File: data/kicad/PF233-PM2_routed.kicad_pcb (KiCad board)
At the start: 4 copper layers, 28 x 70 mm, 17 parts, among them J1 MT60-M leads: BAT+ BAT- ILK, J3 Power switch pair (top housin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, Q1 Si4401FDY -40V

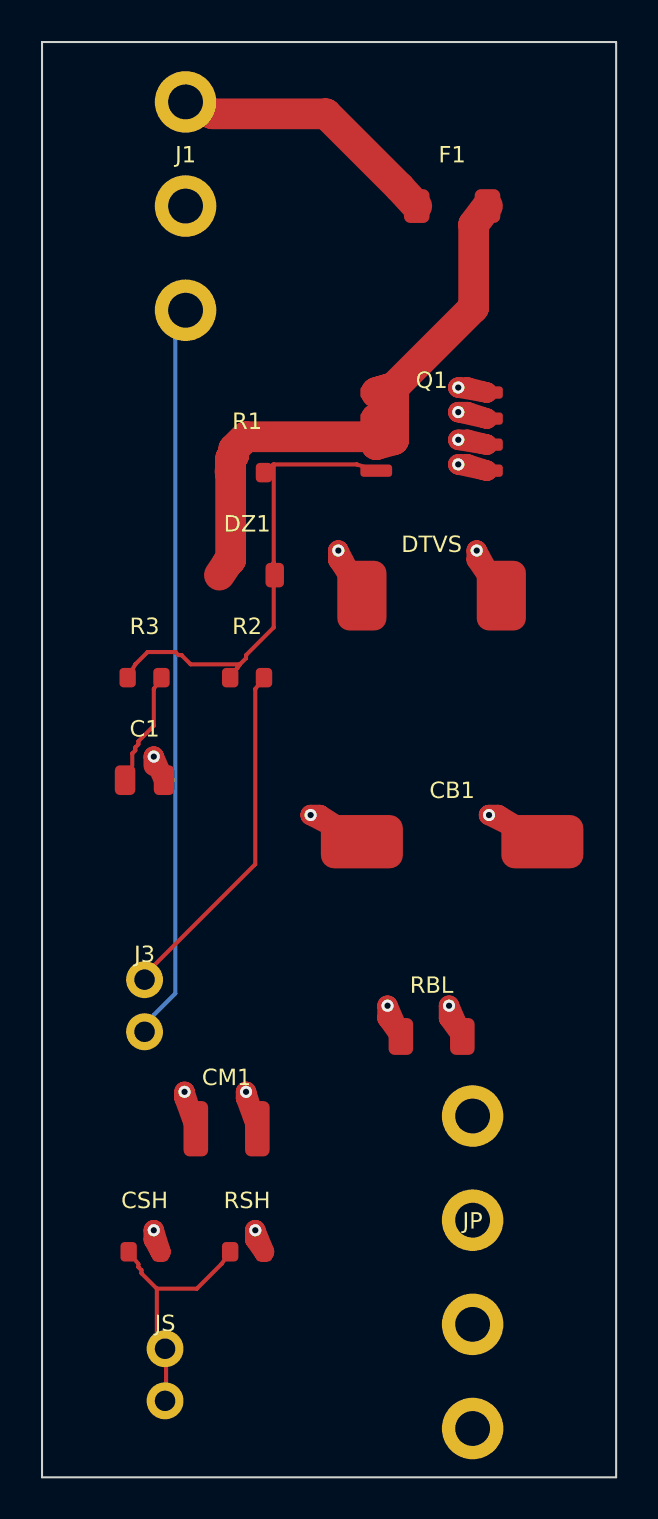
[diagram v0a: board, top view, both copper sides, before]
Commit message: WIP (NOT signed off): data published by the first close-out sign-off run, which had 5 FAIL (CB1D-C2 / AU1 fine-pitch clearance); superseded by the rerun in progress
Co-Authored-By: Claude Opus 5.5 <noreply@anthropic.com>
Claude-Session: https://claude.ai/code/session_01FX4DWSYYjMCFGGA6gmha65
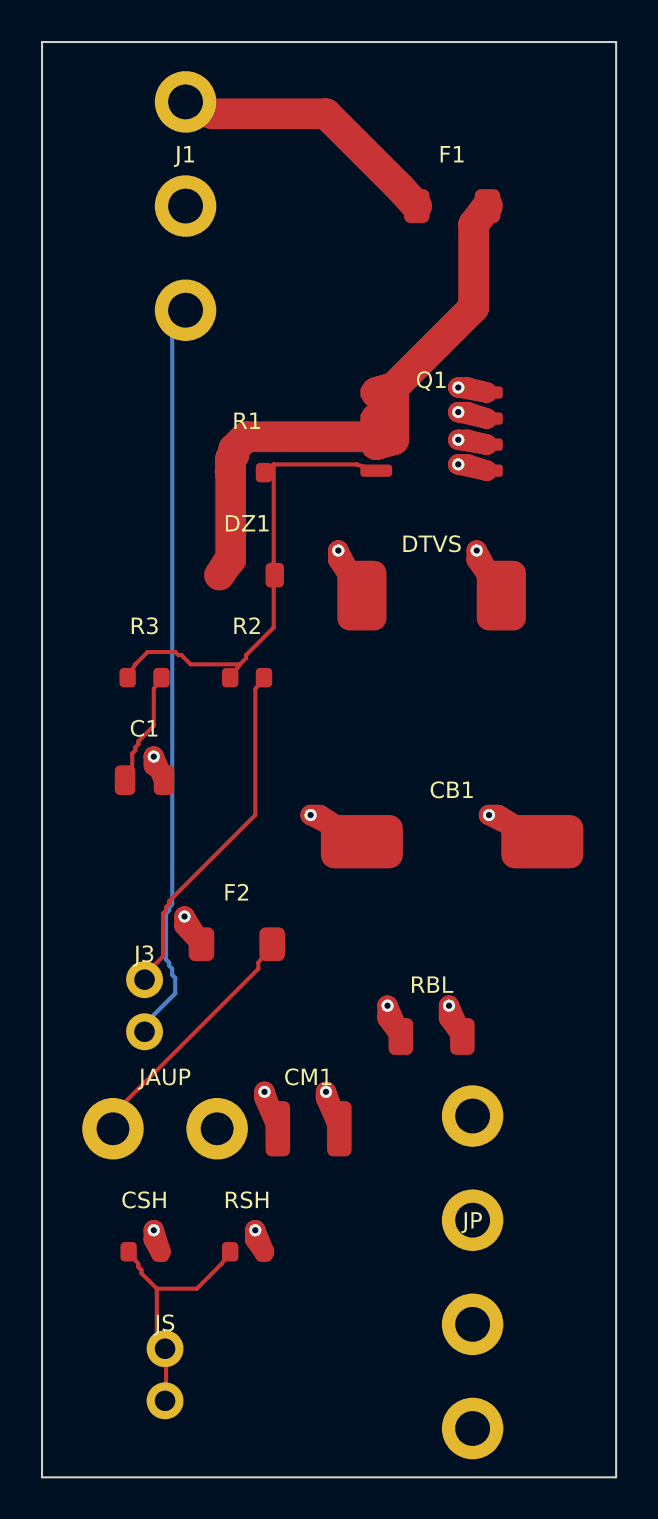
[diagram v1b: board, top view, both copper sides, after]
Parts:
- added F2: 0.5A slow 32V, Fuse:Fuse_1206_3216Metric, F.Cu at (95.5, 109.0)
- added JAUP: Power to AU1: VBUS_AU, GND, Connector:SolderPad_2x_P5.08mm, F.Cu at (92.0, 118.0)
- moved CM1 4.00 mm to (99.0, 118.0)
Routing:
- net VBUS_AU: track 0.00 -> 12.0 mm
- net VBUS: track 31.0 -> 34.3 mm, vias 9 -> 10
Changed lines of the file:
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@@
   (net 8 "SW_A")
   (net 9 "VBUS")
+  (net 10 "VBUS_AU")
   (footprint "Connector:Wire_pads_1x3_P5.08mm" (layer "F.Cu") (at 93.0000 73.0000)
     (property "Reference" "J1" (at 0 -2.5 0) (layer "F.SilkS") (effects (font (size 0.8 0.8) (thickness 0.12))))
@@
     (pad "2" smd roundrect (at 4.400 0.000) (size 4.000 2.600) (layers "F.Cu" "F.Paste" "F.Mask") (net 3 "GND"))
   )
-  (footprint "Capacitor_SMD:C_1210_3225Metric" (layer "F.Cu") (at 95.0000 118.0000)
+  (footprint "Capacitor_SMD:C_1210_3225Metric" (layer "F.Cu") (at 99.0000 118.0000)
     (property "Reference" "CM1" (at 0 -2.5 0) (layer "F.SilkS") (effects (font (size 0.8 0.8) (thickness 0.12))))
     (property "Value" "10u 50V" (at 0 2.5 0) (layer "F.Fab") (effects (font (size 0.8 0.8) (thickness 0.12))))
@@
     (pad "1" smd roundrect (at -1.500 0.000) (size 1.200 1.800) (layers "F.Cu" "F.Paste" "F.Mask") (net 9 "VBUS"))
     (pad "2" smd roundrect (at 1.500 0.000) (size 1.200 1.800) (layers "F.Cu" "F.Paste" "F.Mask") (net 3 "GND"))
+  )
+  (footprint "Fuse:Fuse_1206_3216Metric" (layer "F.Cu") (at 95.5000 109.0000)
+    (property "Reference" "F2" (at 0 -2.5 0) (layer "F.SilkS") (effects (font (size 0.8 0.8) (thickness 0.12))))
+    (property "Value" "0.5A slow 32V" (at 0 2.5 0) (layer "F.Fab") (effects (font (size 0.8 0.8) (thickness 0.12))))
+    (attr smd)
+    (model "${KIPRJMOD}/3dmodels/PF233_FUSE1206B.wrl" (offset (xyz 0 0 0)) (scale (xyz 0.3937 0.3937 0.3937)) (rotate (xyz 0 0 0)))
+    (pad "1" smd roundrect (at -1.725 0.000) (size 1.250 1.650) (layers "F.Cu" "F.Paste" "F.Mask") (net 9 "VBUS"))
+    (pad "2" smd roundrect (at 1.725 0.000) (size 1.250 1.650) (layers "F.Cu" "F.Paste" "F.Mask") (net 10 "VBUS_AU"))
+  )
+  (footprint "Connector:SolderPad_2x_P5.08mm" (layer "F.Cu") (at 92.0000 118.0000)
+    (property "Reference" "JAUP" (at 0 -2.5 0) (layer "F.SilkS") (effects (font (size 0.8 0.8) (thickness 0.12))))
+    (property "Value" "Power to AU1: VBUS_AU, GND" (at 0 2.5 0) (layer "F.Fab") (effects (font (size 0.8 0.8) (thickness 0.12))))
+    (attr through_hole)
+    (pad "1" thru_hole circle (at -2.540 0.000) (size 3.0 3.0) (drill 1.6) (layers "*.Cu" "*.Mask") (net 10 "VBUS_AU"))
+    (pad "2" thru_hole circle (at 2.540 0.000) (size 3.0 3.0) (drill 1.6) (layers "*.Cu" "*.Mask") (net 3 "GND"))
   )
   (footprint "Connector:Wire_pads_1x4_P5.08mm" (layer "F.Cu") (at 107.0000 125.0000)
@@
   (segment (start 108.2500 102.7000) (end 107.8000 102.7000) (width 1.0) (layer "F.Cu") (net 3))
   (segment (start 107.8000 102.7000) (end 110.4000 104.0000) (width 1.0) (layer "F.Cu") (net 3))
-  (segment (start 96.5000 118.0000) (end 95.9500 116.5000) (width 1.0) (layer "F.Cu") (net 3))
-  (segment (start 95.9500 116.5000) (end 95.9500 116.2000) (width 1.0) (layer "F.Cu") (net 3))
-  (segment (start 95.9500 116.2000) (end 96.5000 118.0000) (width 1.0) (layer "F.Cu") (net 3))
+  (segment (start 100.5000 118.0000) (end 99.8500 116.5000) (width 1.0) (layer "F.Cu") (net 3))
+  (segment (start 99.8500 116.5000) (end 99.8500 116.2000) (width 1.0) (layer "F.Cu") (net 3))
+  (segment (start 99.8500 116.2000) (end 100.5000 118.0000) (width 1.0) (layer "F.Cu") (net 3))
   (segment (start 106.5000 113.5000) (end 105.8500 112.6000) (width 1.0) (layer "F.Cu") (net 3))
   (segment (start 105.8500 112.6000) (end 105.8500 112.0000) (width 1.0) (layer "F.Cu") (net 3))
@@
   (segment (start 99.5500 102.7000) (end 99.1000 102.7000) (width 1.0) (layer "F.Cu") (net 9))
   (segment (start 99.1000 102.7000) (end 101.6000 104.0000) (width 1.0) (layer "F.Cu") (net 9))
-  (segment (start 93.5000 118.0000) (end 92.9500 116.5000) (width 1.0) (layer "F.Cu") (net 9))
-  (segment (start 92.9500 116.5000) (end 92.9500 116.2000) (width 1.0) (layer "F.Cu") (net 9))
-  (segment (start 92.9500 116.2000) (end 93.5000 118.0000) (width 1.0) (layer "F.Cu") (net 9))
+  (segment (start 97.5000 118.0000) (end 96.8500 116.5000) (width 1.0) (layer "F.Cu") (net 9))
+  (segment (start 96.8500 116.5000) (end 96.8500 116.2000) (width 1.0) (layer "F.Cu") (net 9))
+  (segment (start 96.8500 116.2000) (end 97.5000 118.0000) (width 1.0) (layer "F.Cu") (net 9))
   (segment (start 103.5000 113.5000) (end 102.8500 112.6000) (width 1.0) (layer "F.Cu") (net 9))
   (segment (start 102.8500 112.6000) (end 102.8500 112.0000) (width 1.0) (layer "F.Cu") (net 9))
   (segment (start 102.8500 112.0000) (end 103.5000 113.5000) (width 1.0) (layer "F.Cu") (net 9))
+  (segment (start 93.7750 109.0000) (end 92.9500 108.1000) (width 1.0) (layer "F.Cu") (net 9))
+  (segment (start 92.9500 108.1000) (end 92.9500 107.6500) (width 1.0) (layer "F.Cu") (net 9))
+  (segment (start 92.9500 107.6500) (end 93.7750 109.0000) (width 1.0) (layer "F.Cu") (net 9))
   (segment (start 93.0000 67.9200) (end 94.3000 68.5000) (width 1.5) (layer "F.Cu") (net 2))
   (segment (start 94.3000 68.5000) (end 99.8500 68.5000) (width 1.5) (layer "F.Cu") (net 2))
@@
   (segment (start 93.5500 125.8000) (end 94.7500 124.6000) (width 0.2) (layer "F.Cu") (net 6))
   (segment (start 94.7500 124.6000) (end 95.1750 124.0000) (width 0.2) (layer "F.Cu") (net 6))
+  (segment (start 97.2250 109.0000) (end 96.5500 109.9000) (width 0.2) (layer "F.Cu") (net 10))
+  (segment (start 96.5500 109.9000) (end 96.5500 110.2000) (width 0.2) (layer "F.Cu") (net 10))
+  (segment (start 96.5500 110.2000) (end 90.1000 116.6500) (width 0.2) (layer "F.Cu") (net 10))
+  (segment (start 90.1000 116.6500) (end 89.4600 118.0000) (width 0.2) (layer "F.Cu") (net 10))
   (segment (start 96.8250 96.0000) (end 96.4000 96.5500) (width 0.2) (layer "F.Cu") (net 8))
-  (segment (start 96.4000 96.5500) (end 96.4000 105.1000) (width 0.2) (layer "F.Cu") (net 8))
-  (segment (start 96.4000 105.1000) (end 91.4500 110.0500) (width 0.2) (layer "F.Cu") (net 8))
+  (segment (start 96.4000 96.5500) (end 96.4000 102.7000) (width 0.2) (layer "F.Cu") (net 8))
+  (segment (start 96.4000 102.7000) (end 92.2000 106.9000) (width 0.2) (layer "F.Cu") (net 8))
+  (segment (start 92.2000 106.9000) (end 92.2000 107.0500) (width 0.2) (layer "F.Cu") (net 8))
+  (segment (start 92.2000 107.0500) (end 92.0500 107.2000) (width 0.2) (layer "F.Cu") (net 8))
+  (segment (start 92.0500 107.2000) (end 92.0500 107.3500) (width 0.2) (layer "F.Cu") (net 8))
+  (segment (start 92.0500 107.3500) (end 91.9000 107.5000) (width 0.2) (layer "F.Cu") (net 8))
+  (segment (start 91.9000 107.5000) (end 91.9000 109.6000) (width 0.2) (layer "F.Cu") (net 8))
+  (segment (start 91.9000 109.6000) (end 91.4500 110.0500) (width 0.2) (layer "F.Cu") (net 8))
   (segment (start 91.4500 110.0500) (end 91.0000 110.7300) (width 0.2) (layer "F.Cu") (net 8))
   (segment (start 102.3000 85.9050) (end 101.3500 85.6000) (width 0.2) (layer "F.Cu") (net 5))
@@
   (segment (start 91.1500 94.7500) (end 90.5500 95.3500) (width 0.2) (layer "F.Cu") (net 5))
   (segment (start 90.5500 95.3500) (end 90.1750 96.0000) (width 0.2) (layer "F.Cu") (net 5))
-  (segment (start 93.0000 78.0800) (end 92.5000 79.4500) (width 0.2) (layer "B.Cu") (net 4))
-  (segment (start 92.5000 79.4500) (end 92.5000 111.4000) (width 0.2) (layer "B.Cu") (net 4))
+  (segment (start 93.0000 78.0800) (end 92.3500 79.4500) (width 0.2) (layer "B.Cu") (net 4))
+  (segment (start 92.3500 79.4500) (end 92.3500 107.0500) (width 0.2) (layer "B.Cu") (net 4))
+  (segment (start 92.3500 107.0500) (end 92.2000 107.2000) (width 0.2) (layer "B.Cu") (net 4))
+  (segment (start 92.2000 107.2000) (end 92.2000 107.3500) (width 0.2) (layer "B.Cu") (net 4))
+  (segment (start 92.2000 107.3500) (end 92.0500 107.5000) (width 0.2) (layer "B.Cu") (net 4))
+  (segment (start 92.0500 107.5000) (end 92.0500 109.7500) (width 0.2) (layer "B.Cu") (net 4))
+  (segment (start 92.0500 109.7500) (end 92.2000 109.9000) (width 0.2) (layer "B.Cu") (net 4))
+  (segment (start 92.2000 109.9000) (end 92.2000 110.0500) (width 0.2) (layer "B.Cu") (net 4))
+  (segment (start 92.2000 110.0500) (end 92.3500 110.2000) (width 0.2) (layer "B.Cu") (net 4))
+  (segment (start 92.3500 110.2000) (end 92.3500 110.5000) (width 0.2) (layer "B.Cu") (net 4))
+  (segment (start 92.3500 110.5000) (end 92.5000 110.6500) (width 0.2) (layer "B.Cu") (net 4))
+  (segment (start 92.5000 110.6500) (end 92.5000 111.4000) (width 0.2) (layer "B.Cu") (net 4))
   (segment (start 92.5000 111.4000) (end 91.4500 112.4500) (width 0.2) (layer "B.Cu") (net 4))
   (segment (start 91.4500 112.4500) (end 91.0000 113.2700) (width 0.2) (layer "B.Cu") (net 4))
   (via (at 107.2000 89.8000) (size 0.6) (drill 0.3) (layers "F.Cu" "B.Cu") (net 3))
   (via (at 107.8000 102.7000) (size 0.6) (drill 0.3) (layers "F.Cu" "B.Cu") (net 3))
-  (via (at 95.9500 116.2000) (size 0.6) (drill 0.3) (layers "F.Cu" "B.Cu") (net 3))
+  (via (at 99.8500 116.2000) (size 0.6) (drill 0.3) (layers "F.Cu" "B.Cu") (net 3))
   (via (at 105.8500 112.0000) (size 0.6) (drill 0.3) (layers "F.Cu" "B.Cu") (net 3))
   (via (at 96.4000 122.9500) (size 0.6) (drill 0.3) (layers "F.Cu" "B.Cu") (net 3))
@@
   (via (at 100.4500 89.8000) (size 0.6) (drill 0.3) (layers "F.Cu" "B.Cu") (net 9))
   (via (at 99.1000 102.7000) (size 0.6) (drill 0.3) (layers "F.Cu" "B.Cu") (net 9))
-  (via (at 92.9500 116.2000) (size 0.6) (drill 0.3) (layers "F.Cu" "B.Cu") (net 9))
+  (via (at 96.8500 116.2000) (size 0.6) (drill 0.3) (layers "F.Cu" "B.Cu") (net 9))
   (via (at 102.8500 112.0000) (size 0.6) (drill 0.3) (layers "F.Cu" "B.Cu") (net 9))
+  (via (at 92.9500 107.6500) (size 0.6) (drill 0.3) (layers "F.Cu" "B.Cu") (net 9))
 )
